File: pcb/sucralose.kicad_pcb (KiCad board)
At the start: 2 copper layers, 154 x 89.9 mm, 96 parts, among them M1 MountingHole_1.2mm_M1

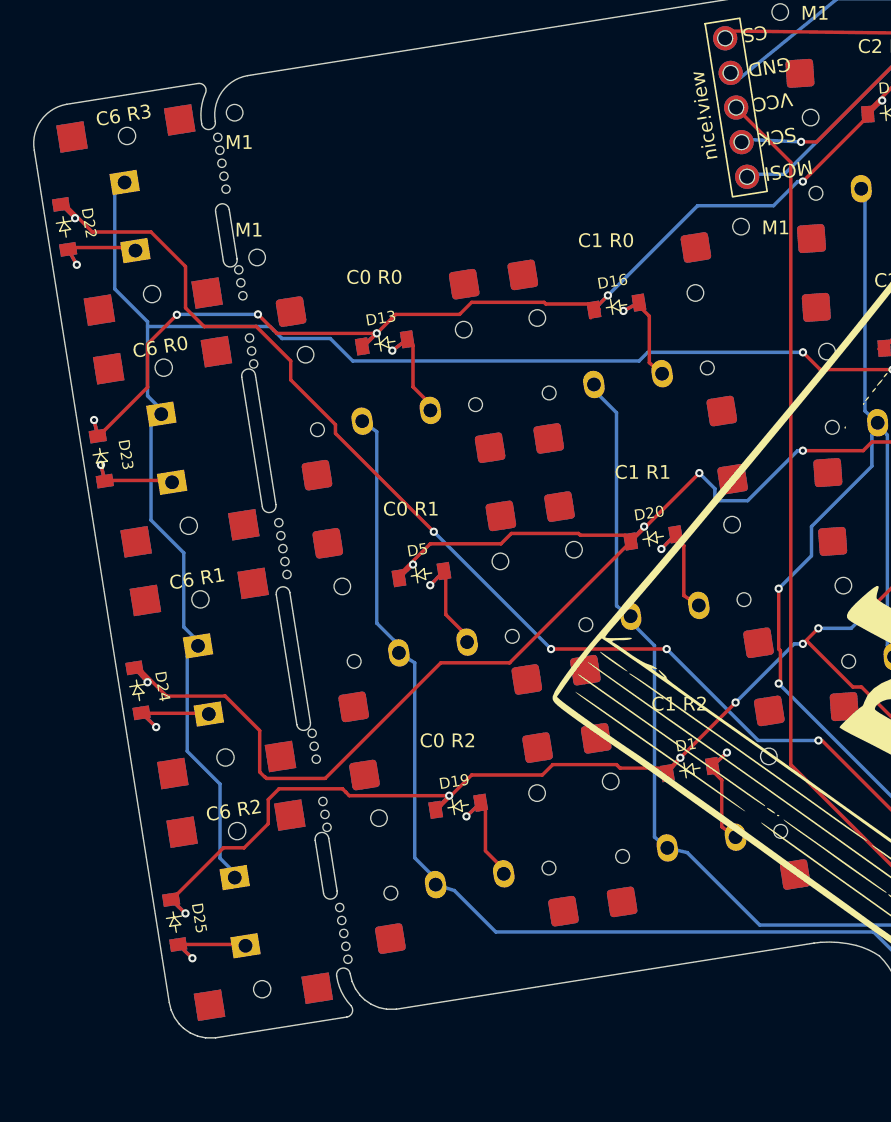
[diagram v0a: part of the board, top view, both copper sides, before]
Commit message: Col7 diodes D22-D25 0.4 mm outboard (with pad-end/tie-via copper and the strip's outer Edge.Cuts): pads now 0.04 mm outside the C6 key courtyards, 0.59 mm to edge kept. Display header M1 +1.0 mm X: (103.648, 71.892). DRC 361, same categories and same 7 unconnected pads.
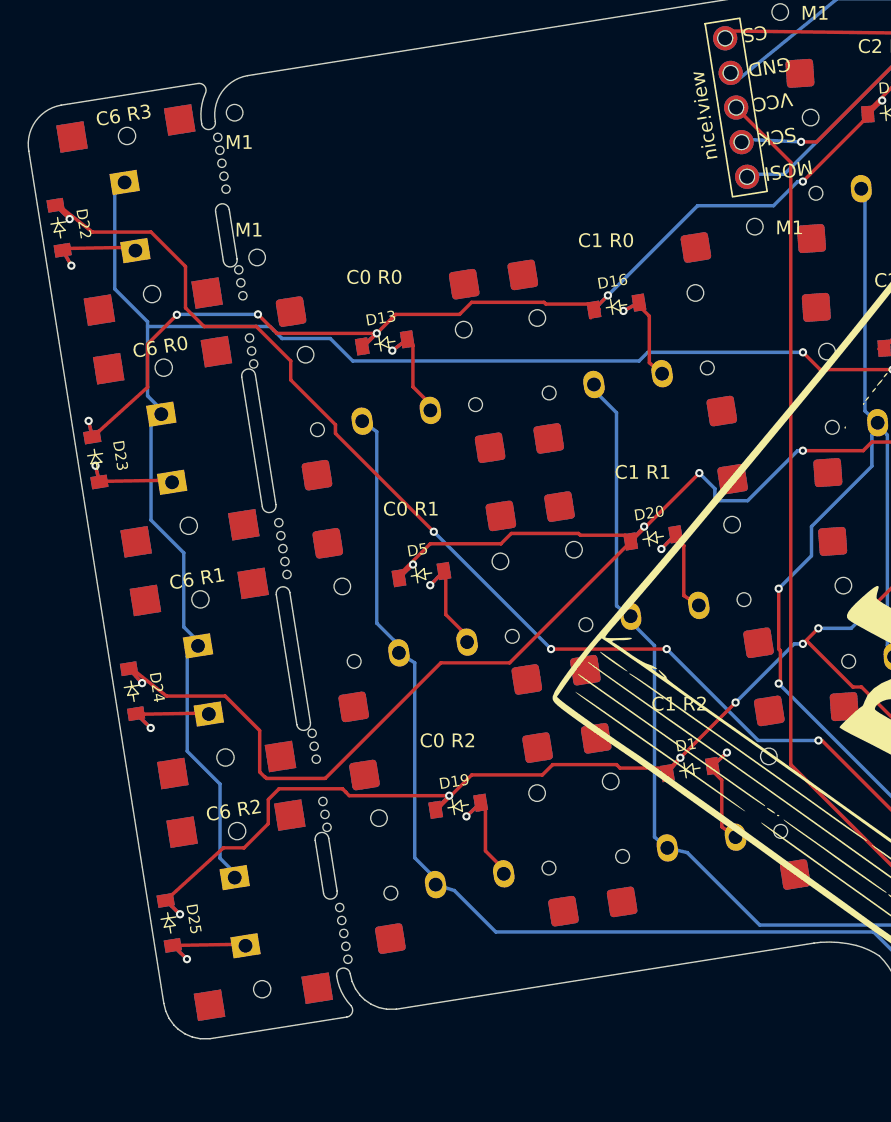
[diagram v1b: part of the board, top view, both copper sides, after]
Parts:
- moved M1 1.00 mm to (103.6, 71.9)
- moved D25 0.40 mm to (61.2, 122.3)
- moved D22 0.40 mm to (53.2, 72.0)
- moved D23 0.40 mm to (55.9, 88.8)
- moved D24 0.40 mm to (58.6, 105.6)
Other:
- board size 154 x 89.9 mm -> 154.3 x 89.9 mm
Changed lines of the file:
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@@
 	(footprint "diode_sod123_reversible"
 		(layer "F.Cu")
-		(at 56.290896 88.700304 -81)
+		(at 55.895821 88.762878 -81)
 		(property "Reference" "D23"
 			(at 0 -1.8 279)
@@
 	(footprint "CustomParts:MountingHole_1.2mm_M1"
 		(layer "F.Cu")
-		(at 102.648 71.892)
+		(at 103.648 71.892)
 		(descr "Mounting Hole 1.2mm, M1, no annular. Courtyard and head outline 2.2 mm dia (ISO 7045 / JIS B 1111 M1-M1.2 pan head dk max 2.0)")
 		(tags "mountinghole M2")
@@
 	(footprint "diode_sod123_reversible"
 		(layer "F.Cu")
-		(at 58.950282 105.491006 -81)
+		(at 58.555207 105.55358 -81)
 		(property "Reference" "D24"
 			(at 0 -1.8 279)
@@
 	(footprint "diode_sod123_reversible"
 		(layer "F.Cu")
-		(at 61.609668 122.281708 -81)
+		(at 61.214593 122.344282 -81)
 		(property "Reference" "D25"
 			(at 0 -1.8 279)
@@
 	(footprint "diode_sod123_reversible"
 		(layer "F.Cu")
-		(at 53.63151 71.909602 -81)
+		(at 53.236435 71.972176 -81)
 		(property "Reference" "D22"
 			(at 0 -1.8 279)
@@
 	)
 	(gr_arc
-		(start 51.435659 66.355732)
-		(mid 51.914742 64.207013)
-		(end 53.773872 63.027985)
+		(start 51.040584 66.418306)
+		(mid 51.519667 64.269587)
+		(end 53.378797 63.090559)
 		(stroke
 			(width 0.1)
@@
 	)
 	(gr_line
-		(start 51.435659 66.355732)
-		(end 61.217349 128.114896)
+		(start 51.040584 66.418306)
+		(end 60.822274 128.17747)
 		(stroke
 			(width 0.1)
@@
 	)
 	(gr_line
-		(start 61.217349 128.114896)
-		(end 61.355432 128.667094)
+		(start 60.822274 128.17747)
+		(end 60.960357 128.729668)
 		(stroke
 			(width 0.1)
@@
 	)
 	(gr_line
-		(start 61.355432 128.667094)
-		(end 61.599041 129.201565)
+		(start 60.960357 128.729668)
+		(end 61.203966 129.264139)
 		(stroke
 			(width 0.1)
@@
 	)
 	(gr_line
-		(start 61.599041 129.201565)
-		(end 61.941762 129.677815)
+		(start 61.203966 129.264139)
+		(end 61.546687 129.740389)
 		(stroke
 			(width 0.1)
@@
 	)
 	(gr_line
-		(start 61.941762 129.677815)
-		(end 62.255758 129.985483)
+		(start 61.546687 129.740389)
+		(end 61.860683 130.048057)
 		(stroke
 			(width 0.1)
@@
 	)
 	(gr_line
-		(start 62.255758 129.985483)
-		(end 62.738882 130.319012)
+		(start 61.860683 130.048057)
+		(end 62.343807 130.381586)
 		(stroke
 			(width 0.1)
@@
 	)
 	(gr_line
-		(start 62.738882 130.319012)
-		(end 63.277896 130.551555)
+		(start 62.343807 130.381586)
+		(end 62.882821 130.614129)
 		(stroke
 			(width 0.1)
@@
 	)
 	(gr_line
-		(start 63.277896 130.551555)
-		(end 63.852156 130.674231)
+		(start 62.882821 130.614129)
+		(end 63.457081 130.736805)
 		(stroke
 			(width 0.1)
@@
 	(gr_line
 		(start 63.304649 61.518458)
-		(end 53.773872 63.027985)
+		(end 53.378797 63.090559)
 		(stroke
 			(width 0.1)
@@
 	)
 	(gr_line
-		(start 63.852156 130.674231)
-		(end 64.566672 130.672434)
+		(start 63.457081 130.736805)
+		(end 64.171597 130.735008)
 		(stroke
 			(width 0.1)
@@
 	(gr_line
 		(start 74.083196 129.165165)
-		(end 64.566672 130.672434)
+		(end 64.171597 130.735008)
 		(stroke
 			(width 0.1)
@@
 	(segment
 		(start 57.768164 73.405992)
-		(end 54.393164 73.405992)
+		(end 53.998089 73.468566)
 		(width 0.25)
 		(layer "F.Cu")
@@
 	)
 	(segment
-		(start 53.889664 73.539292)
-		(end 54.518164 74.655992)
+		(start 53.494589 73.601866)
+		(end 54.123089 74.718566)
 		(width 0.25)
 		(layer "F.Cu")
@@
 	)
 	(segment
-		(start 54.393164 73.405992)
-		(end 53.889664 73.539292)
+		(start 53.998089 73.468566)
+		(end 53.494589 73.601866)
 		(width 0.25)
 		(layer "F.Cu")
@@
 	)
 	(via
-		(at 54.518164 74.655992)
+		(at 54.123089 74.718566)
 		(size 0.6)
 		(drill 0.3)
@@
 	)
 	(segment
-		(start 53.889664 73.539292)
-		(end 54.518164 74.655992)
+		(start 53.494589 73.601866)
+		(end 54.123089 74.718566)
 		(width 0.25)
 		(layer "B.Cu")
@@
 	(segment
 		(start 60.518164 90.280992)
-		(end 57.018164 90.280992)
+		(end 56.623089 90.343566)
 		(width 0.25)
 		(layer "F.Cu")
@@
 	)
 	(segment
-		(start 57.018164 90.280992)
-		(end 56.548964 90.329992)
+		(start 56.623089 90.343566)
+		(end 56.153889 90.392566)
 		(width 0.25)
 		(layer "F.Cu")
@@
 	)
 	(segment
-		(start 56.548964 90.329992)
-		(end 56.268164 89.155992)
+		(start 56.153889 90.392566)
+		(end 55.873089 89.218566)
 		(width 0.25)
 		(layer "F.Cu")
@@
 	)
 	(via
-		(at 56.268164 89.155992)
+		(at 55.873089 89.218566)
 		(size 0.6)
 		(drill 0.3)
@@
 	)
 	(segment
-		(start 56.548964 90.329992)
-		(end 56.268164 89.155992)
+		(start 56.153889 90.392566)
+		(end 55.873089 89.218566)
 		(width 0.25)
 		(layer "B.Cu")
@@
 	)
 	(segment
-		(start 59.208364 107.120692)
-		(end 60.268164 108.155992)
+		(start 58.813289 107.183266)
+		(end 59.873089 108.218566)
 		(width 0.25)
 		(layer "F.Cu")
@@
 	(segment
 		(start 63.143164 107.155992)
-		(end 59.768164 107.155992)
+		(end 59.373089 107.218566)
 		(width 0.25)
 		(layer "F.Cu")
@@
 	)
 	(segment
-		(start 59.768164 107.155992)
-		(end 59.208364 107.120692)
+		(start 59.373089 107.218566)
+		(end 58.813289 107.183266)
 		(width 0.25)
 		(layer "F.Cu")
@@
 	)
 	(via
-		(at 60.268164 108.155992)
+		(at 59.873089 108.218566)
 		(size 0.6)
 		(drill 0.3)
@@
 	)
 	(segment
-		(start 59.208364 107.120692)
-		(end 60.268164 108.155992)
+		(start 58.813289 107.183266)
+		(end 59.873089 108.218566)
 		(width 0.25)
 		(layer "B.Cu")
@@
 	(segment
 		(start 65.768164 123.905992)
-		(end 62.393164 123.905992)
+		(end 61.998089 123.968566)
 		(width 0.25)
 		(layer "F.Cu")
@@
 	)
 	(segment
-		(start 62.393164 123.905992)
-		(end 61.867764 123.911392)
+		(start 61.998089 123.968566)
+		(end 61.472689 123.973966)
 		(width 0.25)
 		(layer "F.Cu")
@@
 	)
 	(segment
-		(start 61.867764 123.911392)
-		(end 62.893164 124.905992)
+		(start 61.472689 123.973966)
+		(end 62.498089 124.968566)
 		(width 0.25)
 		(layer "F.Cu")
@@
 	)
 	(via
-		(at 62.893164 124.905992)
+		(at 62.498089 124.968566)
 		(size 0.6)
 		(drill 0.3)
@@
 	)
 	(segment
-		(start 61.867764 123.911392)
-		(end 62.893164 124.905992)
+		(start 61.472689 123.973966)
+		(end 62.498089 124.968566)
 		(width 0.25)
 		(layer "B.Cu")
@@
 	)
 	(segment
-		(start 53.893164 70.530992)
+		(start 53.498089 70.593566)
 		(end 55.643164 72.280992)
 		(width 0.25)
@@
 	)
 	(segment
-		(start 53.373364 70.279892)
-		(end 54.393164 71.280992)
+		(start 52.978289 70.342466)
+		(end 53.998089 71.343566)
 		(width 0.25)
 		(layer "F.Cu")
@@
 	)
 	(segment
-		(start 53.373364 70.279892)
-		(end 53.893164 70.530992)
+		(start 52.978289 70.342466)
+		(end 53.498089 70.593566)
 		(width 0.25)
 		(layer "F.Cu")
@@
 	)
 	(via
-		(at 54.393164 71.280992)
+		(at 53.998089 71.343566)
 		(size 0.6)
 		(drill 0.3)
@@
 	)
 	(segment
-		(start 53.373364 70.279892)
-		(end 54.393164 71.280992)
+		(start 52.978289 70.342466)
+		(end 53.998089 71.343566)
 		(width 0.25)
 		(layer "B.Cu")
@@
 	)
 	(segment
-		(start 56.518164 86.655992)
+		(start 56.123089 86.718566)
 		(end 59.643164 83.530992)
 		(width 0.25)
@@
 	)
 	(segment
-		(start 56.032764 87.070592)
-		(end 55.768164 85.905992)
+		(start 55.637689 87.133166)
+		(end 55.373089 85.968566)
 		(width 0.25)
 		(layer "F.Cu")
@@
 	)
 	(segment
-		(start 56.032764 87.070592)
-		(end 56.518164 86.655992)
+		(start 55.637689 87.133166)
+		(end 56.123089 86.718566)
 		(width 0.25)
 		(layer "F.Cu")
@@
 	)
 	(via
-		(at 55.768164 85.905992)
+		(at 55.373089 85.968566)
 		(size 0.6)
 		(drill 0.3)
@@
 	)
 	(segment
-		(start 56.032764 87.070592)
-		(end 55.768164 85.905992)
+		(start 55.637689 87.133166)
+		(end 55.373089 85.968566)
 		(width 0.25)
 		(layer "B.Cu")
@@
 	)
 	(segment
-		(start 58.692164 103.861292)
-		(end 59.268164 104.155992)
+		(start 58.297089 103.923866)
+		(end 58.873089 104.218566)
 		(width 0.25)
 		(layer "F.Cu")
@@
 	)
 	(segment
-		(start 59.268164 104.155992)
+		(start 58.873089 104.218566)
 		(end 61.018164 105.905992)
 		(width 0.25)
@@
 	)
 	(segment
-		(start 58.692164 103.861292)
-		(end 59.643164 104.905992)
+		(start 58.297089 103.923866)
+		(end 59.248089 104.968566)
 		(width 0.25)
 		(layer "F.Cu")
@@
 	)
 	(via
-		(at 59.643164 104.905992)
+		(at 59.248089 104.968566)
 		(size 0.6)
 		(drill 0.3)
@@
 	)
 	(segment
-		(start 58.692164 103.861292)
-		(end 59.643164 104.905992)
+		(start 58.297089 103.923866)
+		(end 59.248089 104.968566)
 		(width 0.25)
 		(layer "B.Cu")
@@
 	)
 	(segment
-		(start 61.351564 120.651992)
-		(end 62.393164 121.655992)
+		(start 60.956489 120.714566)
+		(end 61.998089 121.718566)
 		(width 0.25)
 		(layer "F.Cu")
@@
 	)
 	(segment
-		(start 61.351564 120.651992)
-		(end 61.768164 120.280992)
+		(start 60.956489 120.714566)
+		(end 61.373089 120.343566)
 		(width 0.25)
 		(layer "F.Cu")
@@
 	)
 	(segment
-		(start 61.768164 120.280992)
+		(start 61.373089 120.343566)
 		(end 65.143164 116.905992)
 		(width 0.25)
@@
 	)
 	(via
-		(at 62.393164 121.655992)
+		(at 61.998089 121.718566)
 		(size 0.6)
 		(drill 0.3)
@@
 	)
 	(segment
-		(start 61.351564 120.651992)
-		(end 62.393164 121.655992)
+		(start 60.956489 120.714566)
+		(end 61.998089 121.718566)
 		(width 0.25)
 		(layer "B.Cu")

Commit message: Jumper row VCC, GND, RST at y=105 (top view, L->R x 129.5 / 133.8875 / 138.275, 4.3875 pitch; F and B copies). RST jumper moved off the XIAO bottom edge (was 139.8,127.8). RSTH_A/B/RST fully re-routed; BATH_A/B, BAT_P, GND re-routed locally around the row. Router also closed XIAO pad 28/29 BATH_A/BATH_B pairs. DRC 359 (was 361): unconnected 7 -> 5, no new categories.
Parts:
- moved RST 22.9 mm to (138.3, 105.0) (x2)
- moved GND 4.39 mm to (133.9, 105.0) (x2)
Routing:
- net RSTH_B: track 15.2 -> 85.0 mm, vias 0 -> 9
- net RST: track 4.21 -> 65.6 mm, vias 2 -> 7
- net RSTH_A: track 10.4 -> 66.3 mm, vias 2 -> 5
- net BAT_P: track 86.6 -> 100.4 mm, vias 2 -> 6
- net GND: track 173.6 -> 180.3 mm, vias 7 -> 8
- net BATH_A: track 19.1 -> 16.5 mm, vias 1 -> 2
- net BATH_B: track 20.9 -> 18.8 mm, vias 1 -> 2

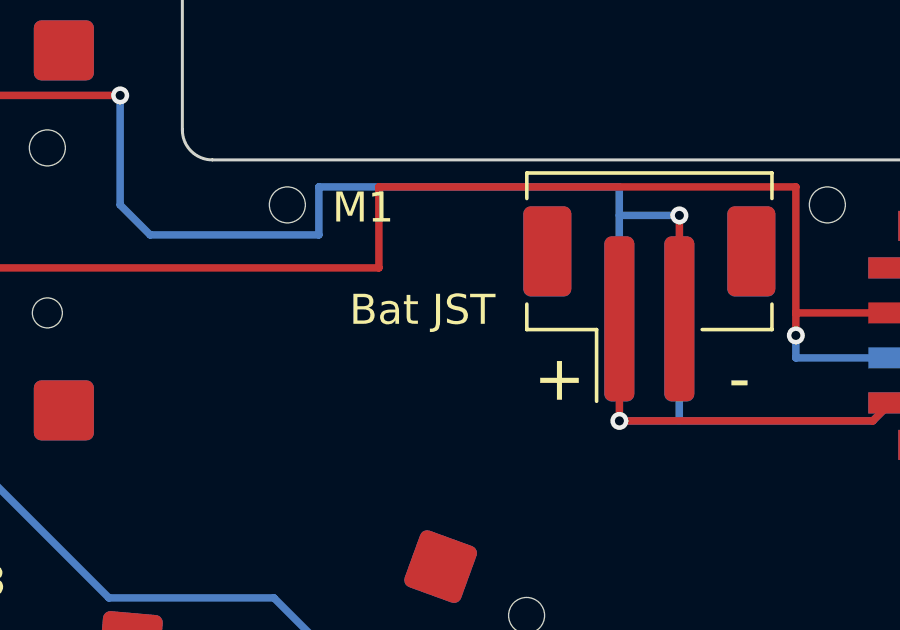
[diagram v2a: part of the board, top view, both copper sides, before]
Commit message: BYP solder jumper (F+B) at (186.75,104.0) across the power switch: pad 1 BAT_P, pad 2 BAT_RAW. Bridge to run without the slide switch (ZMK soft off). BAT_P tapped from the existing F.Cu run at (184.50,103.25) via (185.275,103.25); BAT_RAW joined at the JST + via (192.52,108.35). Bat JST ref silk moved clear. DRC 361: +2 lib_footprint_issues only; unconnected set unchanged.
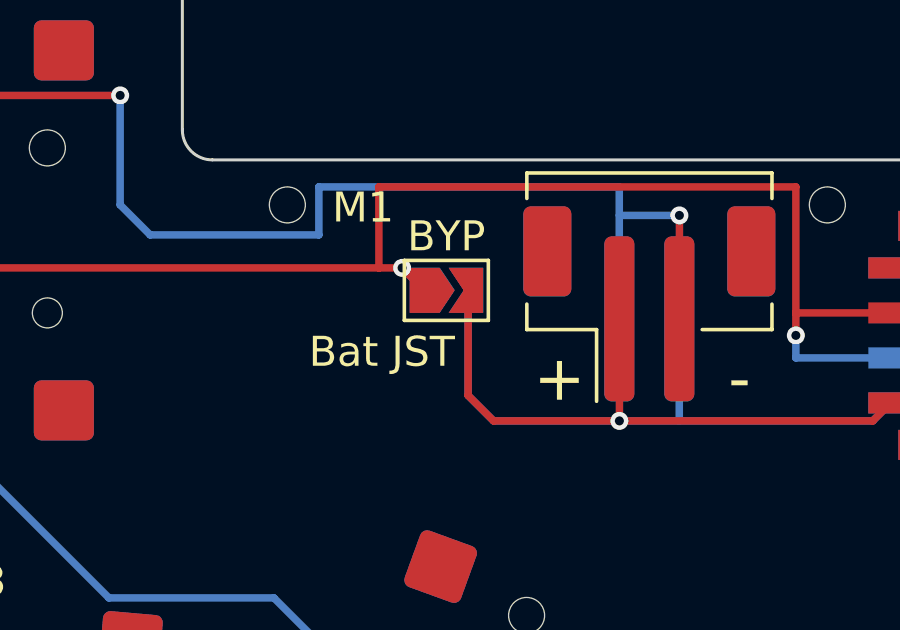
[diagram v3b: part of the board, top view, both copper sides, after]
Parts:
- added BYP: BYP, Jumper:SolderJumper-2_P1.3mm_Open_TrianglePad1.0x1.5mm, F.Cu at (186.8, 104.0)
- added BYP: BYP, Jumper:SolderJumper-2_P1.3mm_Open_TrianglePad1.0x1.5mm, B.Cu at (186.8, 104.0)
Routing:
- net BAT_RAW: track 25.4 -> 43.2 mm
- net BAT_P: track 100.4 -> 103.3 mm, vias 6 -> 7

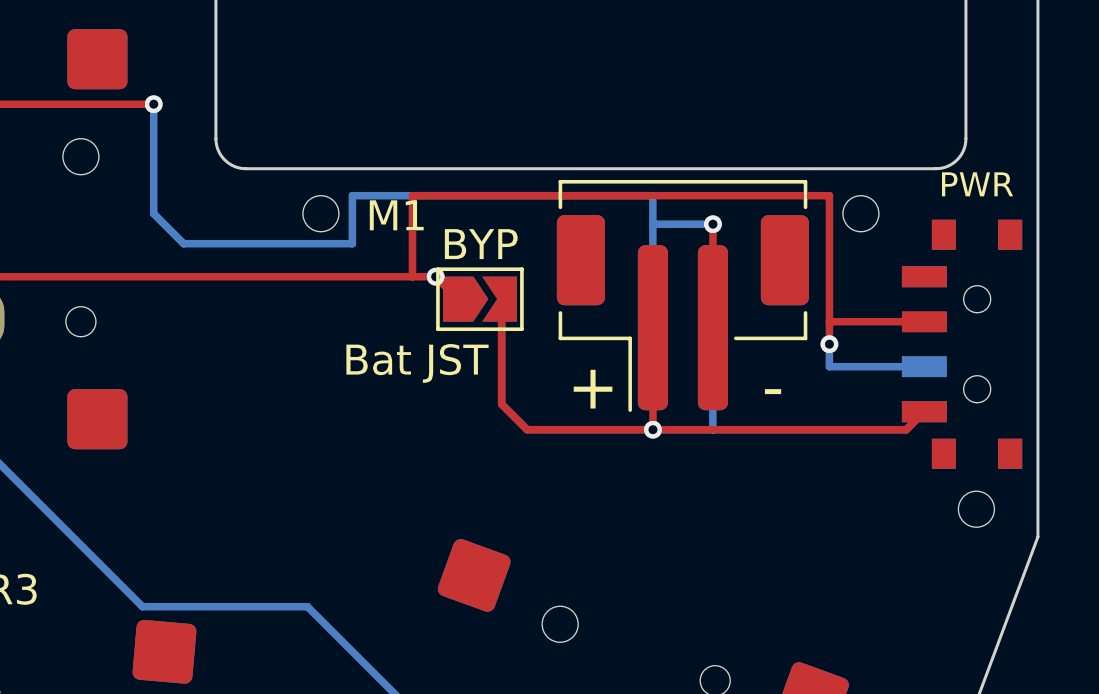
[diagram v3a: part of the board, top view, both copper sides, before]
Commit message: Battery connector: combo land for JST PH S2B-PH-SM4-TB (side entry) OR Molex PicoBlade 53261-0271 (JST MX 1.25), F+B, mating faces toward the battery bay. + (BAT_RAW) stays at x 192.5 (F) / 194.5 (B) as before. BAT_P/BAT_RAW/GND rerouted locally. DRC 362: +2 courtyards_overlap (PH body corner vs C5 R3 keycap outline; real part clears per Jahn), +1 lib_footprint_mismatch (warning); unconnected set unchanged.
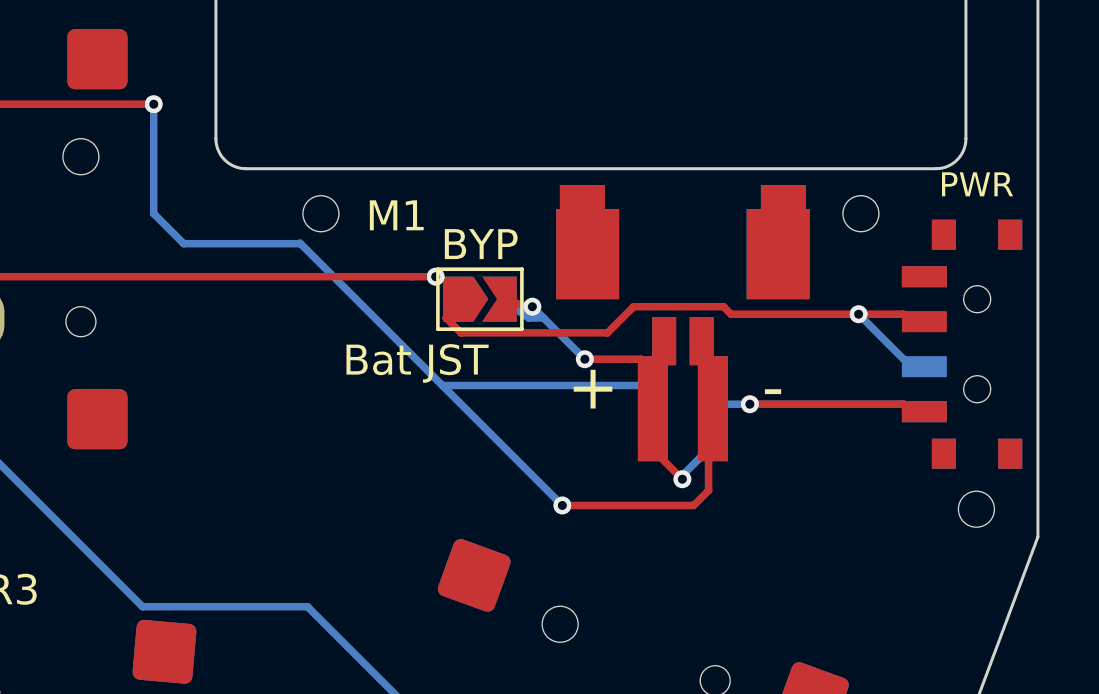
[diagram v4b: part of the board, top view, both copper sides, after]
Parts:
- removed the Bat JST at (193.5, 104.4)
- removed the Bat JST at (193.5, 104.5)
- added Bat JST: PH S2B / PicoBlade 53261, sucralose:BAT_JST-PH-S2B_PicoBlade-53261_SideEntry_sucralose, F.Cu at (193.5, 104.8)
- added Bat JST: PH S2B / PicoBlade 53261, sucralose:BAT_JST-PH-S2B_PicoBlade-53261_SideEntry_sucralose, B.Cu at (193.5, 104.8)
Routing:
- net BAT_RAW: track 43.2 -> 27.0 mm, vias 1 -> 4
- net BAT_P: track 103.3 -> 92.8 mm
- net GND: track 180.3 -> 184.8 mm
